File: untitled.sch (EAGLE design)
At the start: 33 parts, among them J2 1x3 RA Female .1", U1 SI4463-C2A-GM, U2 ATSAMD21G-M

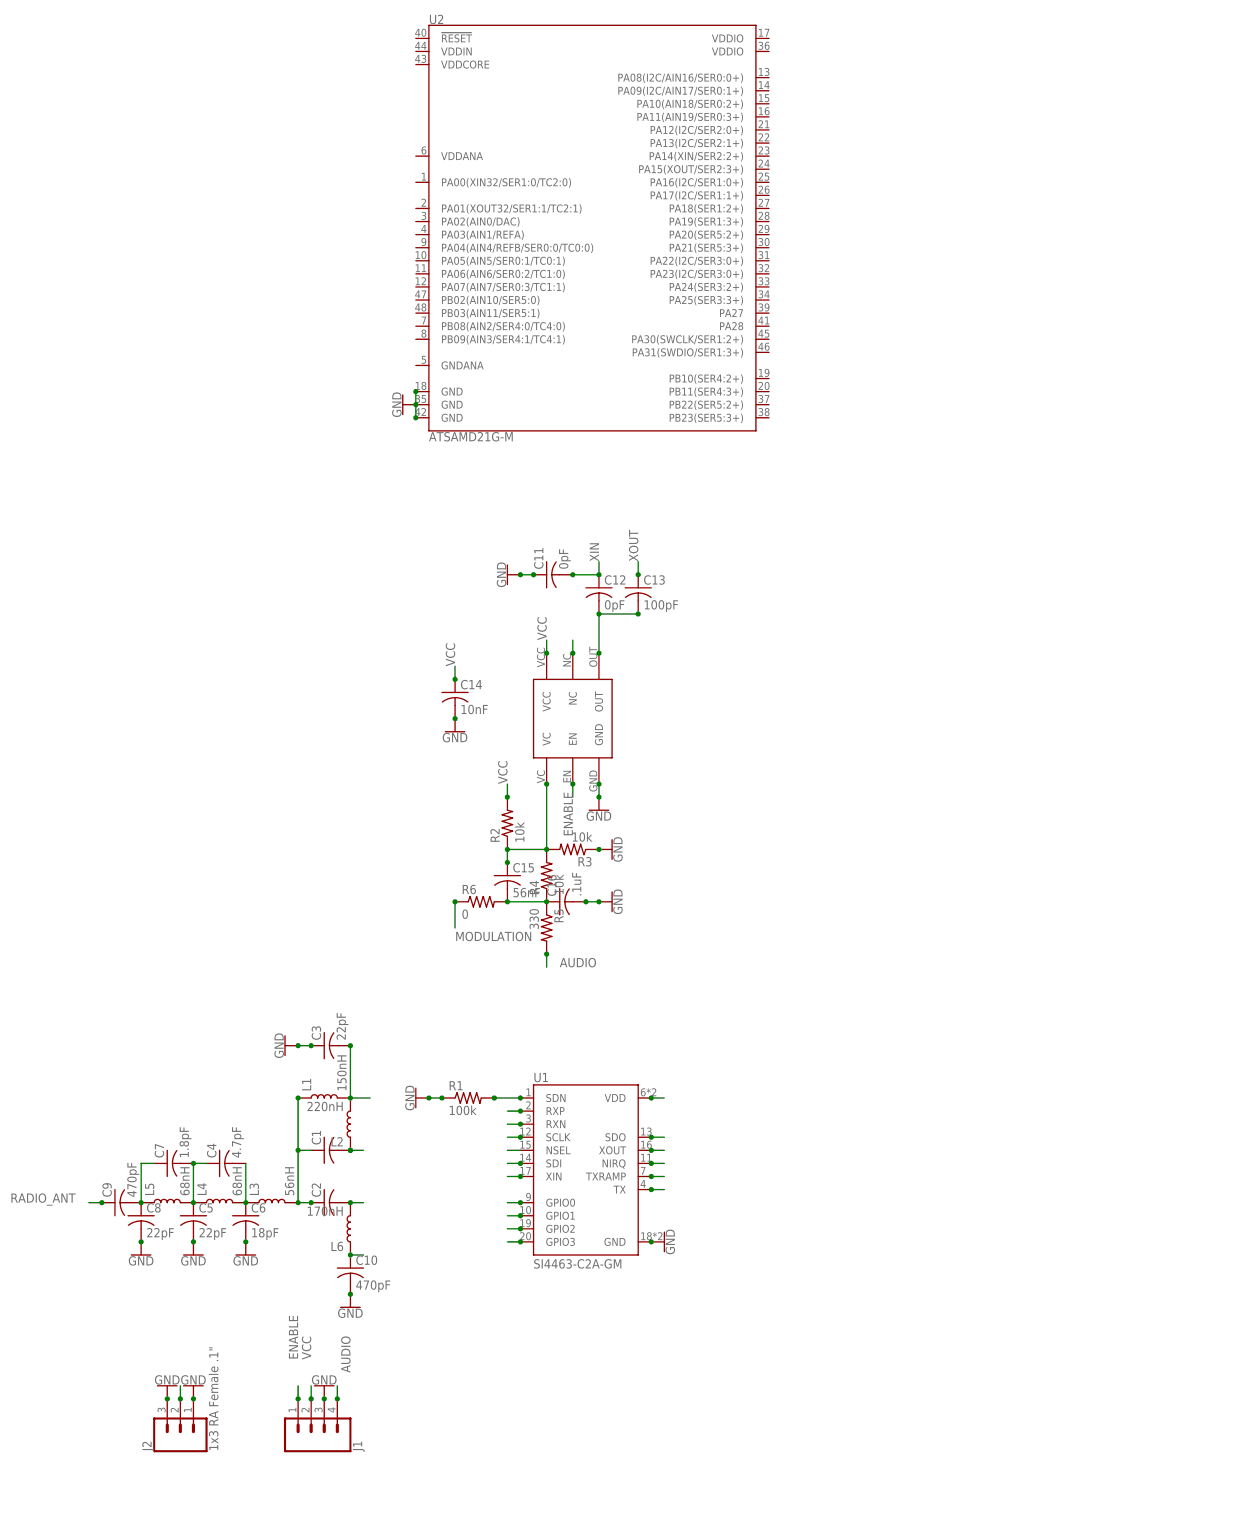
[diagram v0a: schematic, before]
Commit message: initial atsamd21g schematic capture
added samd21g connections.
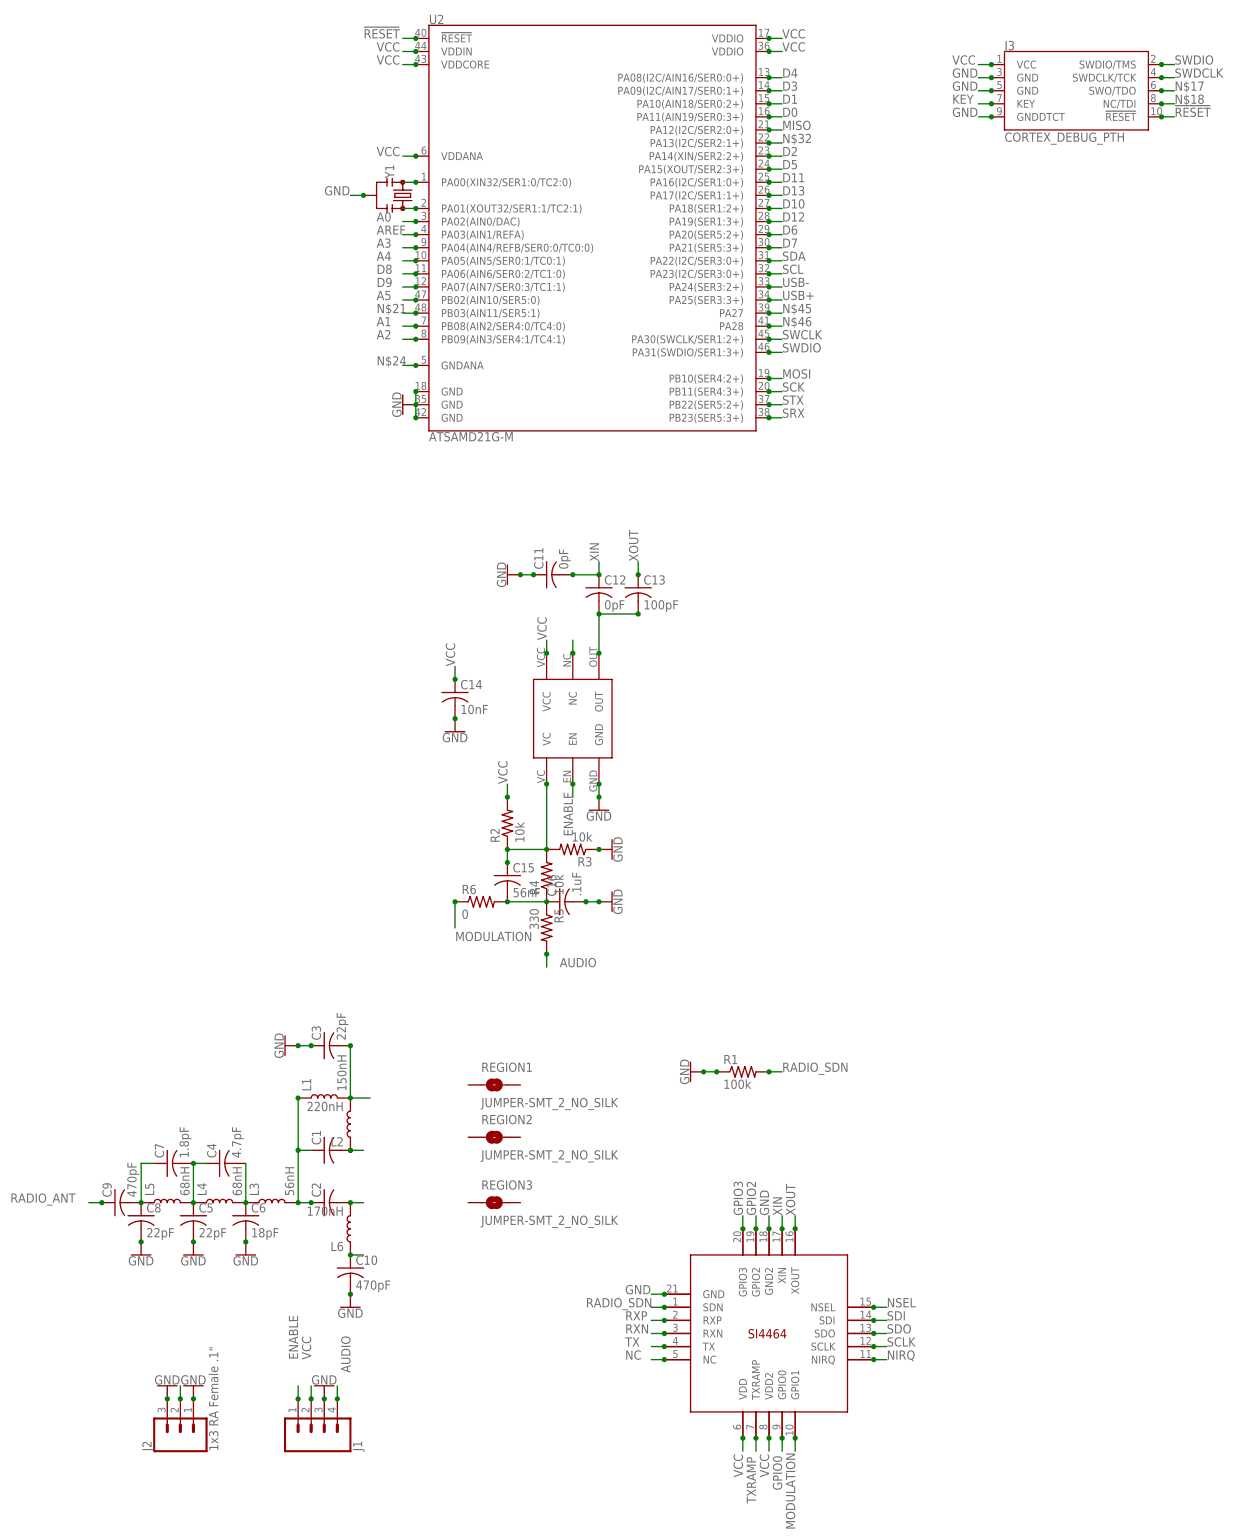
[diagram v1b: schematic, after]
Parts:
- removed U1: SI4463-C2A-GM, SI4463-C2A-GM:SI4463-C2A-GM
- added J3: CORTEX_DEBUG_PTH, SparkFun-Connectors:CORTEX_DEBUG_PTH
- added REGION1, REGION2, REGION3: JUMPER-SMT_2_NO_SILK, SparkFun-Jumpers:JUMPER-SMT_2_NO_SILK
- added U$2: SI4464, Ava:SI4464
- added Y1: (no value), SparkFun-Clocks:RESONATORSMD-3.2X1.3
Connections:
- new net !RESET: J3.!RESET, U2.!RESET!
- new net A0: U2.PA02(AIN0/DAC)
- new net A1: U2.PB08(AIN2/SER4:0/TC4:0)
- new net A2: U2.PB09(AIN3/SER4:1/TC4:1)
- new net A3: U2.PA04(AIN4/REFB/SER0:0/TC0:0)
- new net A4: U2.PA05(AIN5/SER0:1/TC0:1)
- new net A5: U2.PB02(AIN10/SER5:0)
- new net AREF: U2.PA03(AIN1/REFA)
- new net D0: U2.PA11(AIN19/SER0:3+)
- new net D1: U2.PA10(AIN18/SER0:2+)
- new net D10: U2.PA18(SER1:2+)
- new net D11: U2.PA16(I2C/SER1:0+)
- new net D12: U2.PA19(SER1:3+)
- new net D13: U2.PA17(I2C/SER1:1+)
- new net D2: U2.PA14(XIN/SER2:2+)
- new net D3: U2.PA09(I2C/AIN17/SER0:1+)
- new net D4: U2.PA08(I2C/AIN16/SER0:0+)
- new net D5: U2.PA15(XOUT/SER2:3+)
- new net D6: U2.PA20(SER5:2+)
- new net D7: U2.PA21(SER5:3+)
- new net D8: U2.PA06(AIN6/SER0:2/TC1:0)
- new net D9: U2.PA07(AIN7/SER0:3/TC1:1)
- new net KEY: J3.KEY
- new net MISO: U2.PA12(I2C/SER2:0+)
- new net MOSI: U2.PB10(SER4:2+)
- new net N$17: J3.SWO/TDO
- new net N$18: J3.NC/TDI
- new net N$21: U2.PB03(AIN11/SER5:1)
- new net N$24: U2.GNDANA
- new net N$32: U2.PA13(I2C/SER2:1+)
- new net N$45: U2.PA27
- new net N$46: U2.PA28
- new net N$7: U2.PA01(XOUT32/SER1:1/TC2:1), Y1.3
- new net N$8: U2.PA00(XIN32/SER1:0/TC2:0), Y1.1
- new net NC: U$2.NC 
- new net SCK: U2.PB11(SER4:3+)
- new net SCL: U2.PA23(I2C/SER3:0+)
- new net SDA: U2.PA22(I2C/SER3:0+)
- new net SRX: U2.PB23(SER5:3+)
- new net STX: U2.PB22(SER5:2+)
- new net SWCLK: U2.PA30(SWCLK/SER1:2+)
- new net SWDCLK: J3.SWDCLK/TCK
- new net SWDIO: J3.SWDIO/TMS, U2.PA31(SWDIO/SER1:3+)
- new net USB+: U2.PA25(SER3:3+)
- new net USB-: U2.PA24(SER3:2+)
- net GND: now also J3.GND@3, J3.GND@5, J3.GNDDTCT, U$2.GND, U$2.GND2, Y1.2; no longer U1.GND
- net GPIO0: now also U$2.GPIO0; no longer U1.GPIO0
- net GPIO2: now also U$2.GPIO2; no longer U1.GPIO2
- net GPIO3: now also U$2.GPIO3; no longer U1.GPIO3
- net MODULATION: now also U$2.GPIO1; no longer U1.GPIO1
- net NIRQ: now also U$2.NIRQ; no longer U1.NIRQ
- net NSEL: now also U$2.NSEL; no longer U1.NSEL
- net RADIO_SDN: now also U$2.SDN; no longer U1.SDN
- net RXN: now also U$2.RXN; no longer U1.RXN
- net RXP: now also U$2.RXP; no longer U1.RXP
- net SCLK: now also U$2.SCLK; no longer U1.SCLK
- net SDI: now also U$2.SDI; no longer U1.SDI
- net SDO: now also U$2.SDO; no longer U1.SDO
- net TX: now also U$2.TX; no longer U1.TX
- net TXRAMP: now also U$2.TXRAMP; no longer U1.TXRAMP
- net VCC: now also J3.VCC, U$2.VDD, U$2.VDD2, U2.VDDANA, U2.VDDCORE, U2.VDDIN, U2.VDDIO@17, U2.VDDIO@36; no longer U1.VDD
- net XIN: now also U$2.XIN; no longer U1.XIN
- net XOUT: now also U$2.XOUT; no longer U1.XOUT
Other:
- moved on the sheet: R1
